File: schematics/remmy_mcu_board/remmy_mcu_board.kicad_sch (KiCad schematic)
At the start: 25 parts, among them J1 AVR-JTAG-10, J2 Conn_02x05_Counter_Clockwise, J3 Conn_01x03_Pin, Q1 BSS138, SW1 RotaryEncoder, SW2 SW_Push, SW3 SW_Push, SW4 SW_Push, U1 NX3225SA-16, U2 ATmega32U4-M, U3 Kailh GM 8.0, U4 Kailh GM 8.0

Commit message: added images
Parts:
- renumbered SW2 to SW1, SW1 to SW2, SW4 to SW3, SW3 to SW4, U3 to SW5, U4 to SW6, U1 to X1
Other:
- title: (none) -> Remmy A
- moved on the sheet: C1, C2, C3, C4, C5, C6, C7, C8, D1, J1, J2, J3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

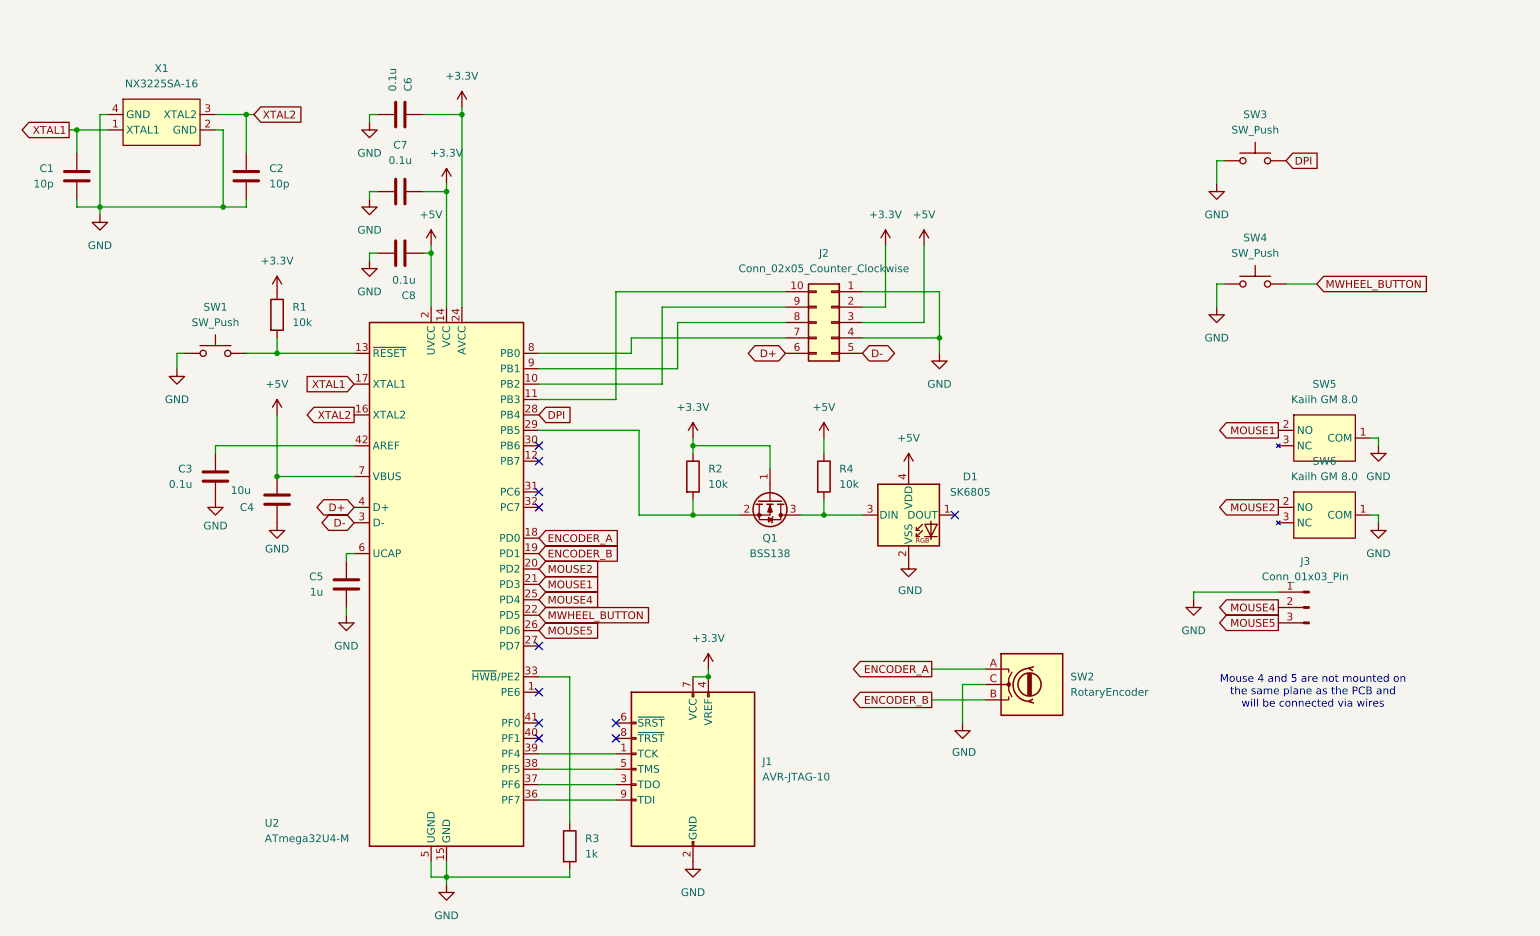
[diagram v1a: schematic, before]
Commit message: broken spi comm
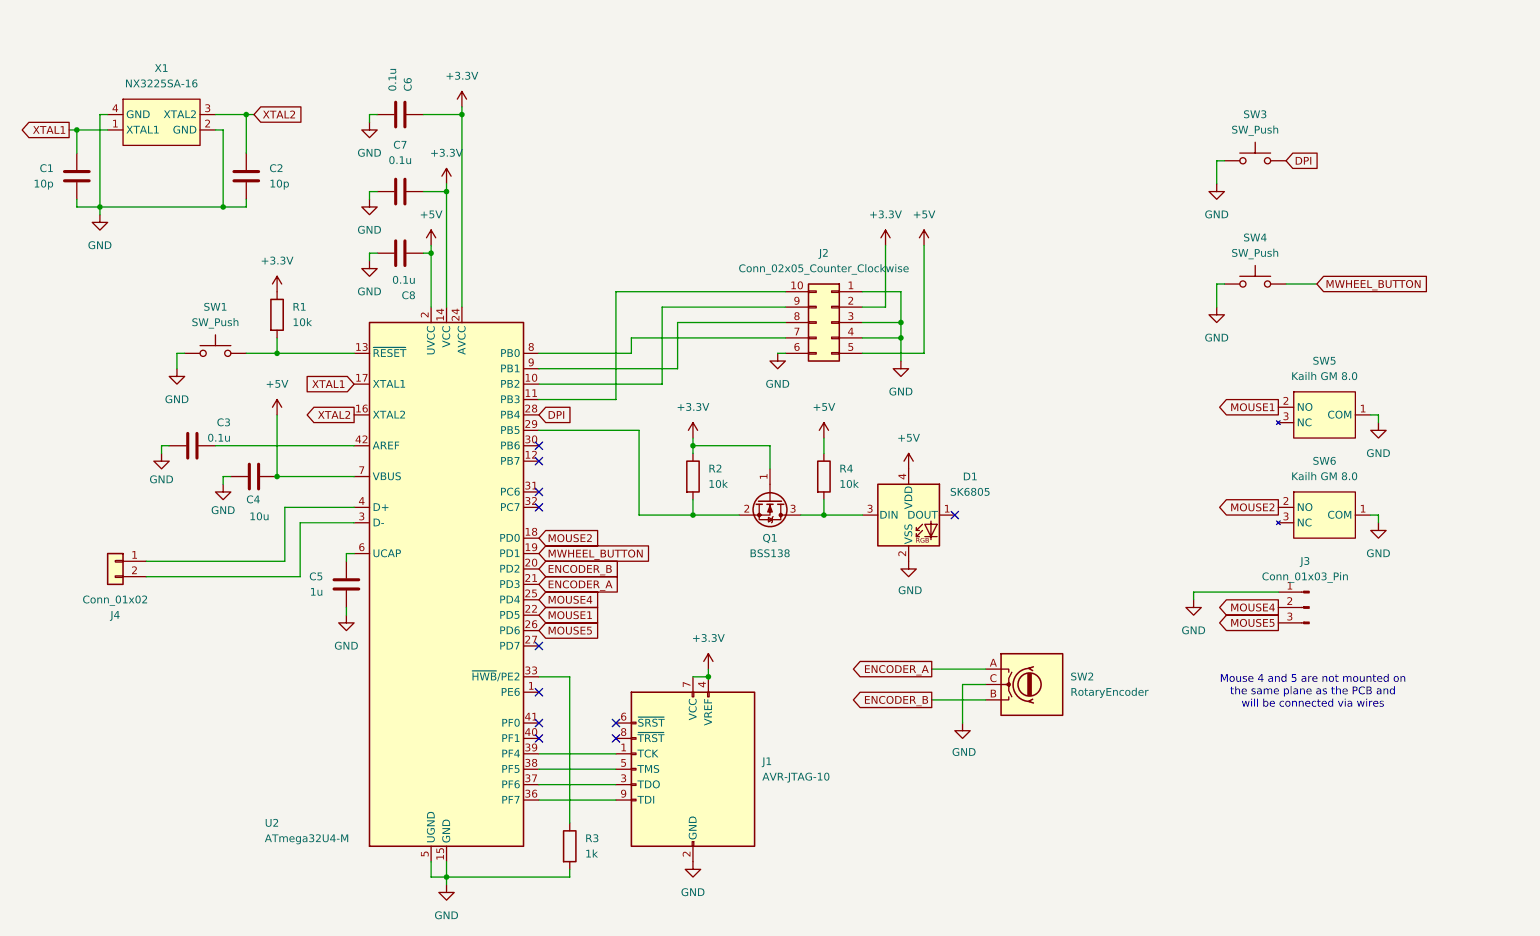
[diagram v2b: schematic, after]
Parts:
- added J4: Conn_01x02, Connector_PinHeader_1.27mm:PinHeader_1x02_P1.27mm_Vertical, symbol Connector_Generic:Conn_01x02
- J3: footprint Connector_PinSocket_2.54mm:PinSocket_1x03_P2.54mm_Vertical -> Connector_PinSocket_1.27mm:PinSocket_1x03_P1.27mm_Vertical
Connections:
- net +5V: now also C4.1, J2.5 (Pin_5); no longer C4.2, J2.3 (Pin_3)
- net ENCODER_A: now also U2.21 (PD3); no longer U2.18 (PD0)
- net ENCODER_B: now also U2.20 (PD2); no longer U2.19 (PD1)
- net GND: now also C3.1, C4.2, J2.3 (Pin_3), J2.6 (Pin_6); no longer C3.2, C4.1
- net MOUSE1: now also U2.22 (PD5); no longer U2.21 (PD3)
- net MOUSE2: now also U2.18 (PD0); no longer U2.20 (PD2)
- net MWHEEL_BUTTON: now also U2.19 (PD1); no longer U2.22 (PD5)
- net at U2.42 (AREF): now also C3.2; no longer C3.1
- net D+: no longer names the net of U2.4 (D+)
- net D+: now also J4.1 (Pin_1); no longer J2.6 (Pin_6)
- net D-: no longer names the net of U2.3 (D-)
- net D-: now also J4.2 (Pin_2); no longer J2.5 (Pin_5)
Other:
- moved on the sheet: C3, C4, SW5
